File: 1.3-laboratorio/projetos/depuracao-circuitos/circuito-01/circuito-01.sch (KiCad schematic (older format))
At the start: 0 parts

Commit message: Atualização do projeto de depuração de circuitos
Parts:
- added D1: LED, LEDs:LED_D3.0mm, symbol LED
- added Entradas1: Conn_01x04, Connectors:Grove_1x04, symbol Conn_01x04
- added R1: R, Resistors_THT:R_Axial_DIN0309_L9.0mm_D3.2mm_P12.70mm_Horizontal, symbol R
- added U1: 74LS32, Housings_DIP:DIP-14_W7.62mm_Socket, symbol 74LS32
- added U2: 7400, Housings_DIP:DIP-14_W7.62mm_Socket, symbol 7400
- added U3: 74LS386, Housings_DIP:DIP-14_W7.62mm_Socket, symbol 74LS386
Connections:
- net labels added: GND
- wire segments 0 -> 47
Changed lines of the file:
@@
 Comment4 ""
 $EndDescr
+$Comp
+L GND #PWR01
+U 1 1 5B0DB24C
+P 9650 4150
+F 0 "#PWR01" H 9650 3900 50  0001 C CNN
+F 1 "GND" H 9650 4000 50  0000 C CNN
+F 2 "" H 9650 4150 50  0001 C CNN
+F 3 "" H 9650 4150 50  0001 C CNN
+	1    9650 4150
+	1    0    0    -1
+$EndComp
+$Comp
+L 7400 U2
+U 1 1 5B0DB2F1
+P 3650 3150
+F 0 "U2" H 3650 3200 50  0000 C CNN
+F 1 "7400" H 3650 3050 50  0000 C CNN
+F 2 "Housings_DIP:DIP-14_W7.62mm_Socket" H 3650 3150 50  0001 C CNN
+F 3 "" H 3650 3150 50  0001 C CNN
+	1    3650 3150
+	1    0    0    -1
+$EndComp
+$Comp
+L 7400 U2
+U 2 1 5B0DB37B
+P 5500 3900
+F 0 "U2" H 5500 3950 50  0000 C CNN
+F 1 "7400" H 5500 3800 50  0000 C CNN
+F 2 "Housings_DIP:DIP-14_W7.62mm_Socket" H 5500 3900 50  0001 C CNN
+F 3 "" H 5500 3900 50  0001 C CNN
+	2    5500 3900
+	1    0    0    -1
+$EndComp
+$Comp
+L 7400 U2
+U 3 1 5B0DB3EE
+P 6900 3900
+F 0 "U2" H 6900 3950 50  0000 C CNN
+F 1 "7400" H 6900 3800 50  0000 C CNN
+F 2 "Housings_DIP:DIP-14_W7.62mm_Socket" H 6900 3900 50  0001 C CNN
+F 3 "" H 6900 3900 50  0001 C CNN
+	3    6900 3900
+	1    0    0    -1
+$EndComp
+$Comp
+L 7400 U2
+U 4 1 5B0DB449
+P 7400 2900
+F 0 "U2" H 7400 2950 50  0000 C CNN
+F 1 "7400" H 7400 2800 50  0000 C CNN
+F 2 "Housings_DIP:DIP-14_W7.62mm_Socket" H 7400 2900 50  0001 C CNN
+F 3 "" H 7400 2900 50  0001 C CNN
+	4    7400 2900
+	1    0    0    -1
+$EndComp
+$Comp
+L 74LS32 U1
+U 1 1 5B0DB788
+P 3650 2450
+F 0 "U1" H 3650 2500 50  0000 C CNN
+F 1 "74LS32" H 3650 2400 50  0000 C CNN
+F 2 "Housings_DIP:DIP-14_W7.62mm_Socket" H 3650 2450 50  0001 C CNN
+F 3 "" H 3650 2450 50  0001 C CNN
+	1    3650 2450
+	1    0    0    -1
+$EndComp
+$Comp
+L 74LS32 U1
+U 2 1 5B0DB7F9
+P 3650 3900
+F 0 "U1" H 3650 3950 50  0000 C CNN
+F 1 "74LS32" H 3650 3850 50  0000 C CNN
+F 2 "Housings_DIP:DIP-14_W7.62mm_Socket" H 3650 3900 50  0001 C CNN
+F 3 "" H 3650 3900 50  0001 C CNN
+	2    3650 3900
+	1    0    0    -1
+$EndComp
+$Comp
+L 74LS32 U1
+U 3 1 5B0DB864
+P 5350 3150
+F 0 "U1" H 5350 3200 50  0000 C CNN
+F 1 "74LS32" H 5350 3100 50  0000 C CNN
+F 2 "Housings_DIP:DIP-14_W7.62mm_Socket" H 5350 3150 50  0001 C CNN
+F 3 "" H 5350 3150 50  0001 C CNN
+	3    5350 3150
+	1    0    0    -1
+$EndComp
+$Comp
+L 74LS386 U3
+U 1 1 5B0DB8C7
+P 8900 3300
+F 0 "U3" H 8900 3350 50  0000 C CNN
+F 1 "74LS386" H 8900 3250 50  0000 C CNN
+F 2 "Housings_DIP:DIP-14_W7.62mm_Socket" H 8900 3300 50  0001 C CNN
+F 3 "" H 8900 3300 50  0001 C CNN
+	1    8900 3300
+	1    0    0    -1
+$EndComp
+$Comp
+L Conn_01x04 Entradas1
+U 1 1 5B0DF1AF
+P 1600 2850
+F 0 "Entradas1" H 1600 3050 50  0000 C CNN
+F 1 "Conn_01x04" H 1600 2550 50  0000 C CNN
+F 2 "Connectors:Grove_1x04" H 1600 2850 50  0001 C CNN
+F 3 "" H 1600 2850 50  0001 C CNN
+	1    1600 2850
+	-1   0    0    -1
+$EndComp
+$Comp
+L LED D1
+U 1 1 5B0DF2B7
+P 9650 3900
+F 0 "D1" H 9650 4000 50  0000 C CNN
+F 1 "LED" H 9650 3800 50  0000 C CNN
+F 2 "LEDs:LED_D3.0mm" H 9650 3900 50  0001 C CNN
+F 3 "" H 9650 3900 50  0001 C CNN
+	1    9650 3900
+	0    -1   -1   0
+$EndComp
+$Comp
+L R R1
+U 1 1 5B0DF334
+P 9650 3500
+F 0 "R1" V 9730 3500 50  0000 C CNN
+F 1 "R" V 9650 3500 50  0000 C CNN
+F 2 "Resistors_THT:R_Axial_DIN0309_L9.0mm_D3.2mm_P12.70mm_Horizontal" V 9580 3500 50  0001 C CNN
+F 3 "" H 9650 3500 50  0001 C CNN
+	1    9650 3500
+	1    0    0    -1
+$EndComp
+Wire Wire Line
+	1800 2750 2350 2750
+Wire Wire Line
+	2350 2750 2350 2350
+Wire Wire Line
+	2350 2350 3050 2350
+Wire Wire Line
+	1800 2850 2500 2850
+Wire Wire Line
+	2500 2850 2500 2550
+Wire Wire Line
+	2500 2550 3050 2550
+Wire Wire Line
+	2900 2350 2900 3050
+Wire Wire Line
+	2900 3050 3050 3050
+Connection ~ 2900 2350
+Wire Wire Line
+	1800 2950 2750 2950
+Wire Wire Line
+	2750 2950 2750 3250
+Wire Wire Line
+	2750 3250 3050 3250
+Wire Wire Line
+	1800 3050 2600 3050
+Wire Wire Line
+	2600 3050 2600 4000
+Wire Wire Line
+	2600 4000 3050 4000
+Wire Wire Line
+	2700 2550 2700 3800
+Wire Wire Line
+	2700 3800 3050 3800
+Connection ~ 2700 2550
+Wire Wire Line
+	4250 3150 4500 3150
+Wire Wire Line
+	4500 3150 4500 3250
+Wire Wire Line
+	4500 3250 4750 3250
+Wire Wire Line
+	4750 3050 4750 2450
+Wire Wire Line
+	4250 2450 6150 2450
+Wire Wire Line
+	6800 2800 6150 2800
+Wire Wire Line
+	6150 2800 6150 2450
+Connection ~ 4750 2450
+Wire Wire Line
+	6800 3000 6300 3000
+Wire Wire Line
+	6300 3000 6300 3150
+Wire Wire Line
+	6300 3150 5950 3150
+Wire Wire Line
+	4250 3900 4450 3900
+Wire Wire Line
+	4450 3900 4450 4000
+Wire Wire Line
+	4450 4000 4900 4000
+Wire Wire Line
+	6250 3800 6250 4000
+Wire Wire Line
+	5300 3750 5350 3750
+Wire Wire Line
+	6250 4000 6300 4000
+Connection ~ 6250 3900
+Wire Wire Line
+	6150 3150 6150 3600
+Wire Wire Line
+	6150 3600 4900 3600
+Wire Wire Line
+	4900 3600 4900 3800
+Connection ~ 6150 3150
+Wire Wire Line
+	8300 3200 8200 3200
+Wire Wire Line
+	8200 3200 8200 2900
+Wire Wire Line
+	8200 2900 8000 2900
+Wire Wire Line
+	8300 3400 8200 3400
+Wire Wire Line
+	8200 3400 8200 3900
+Wire Wire Line
+	9650 3300 9650 3350
+Wire Wire Line
+	9650 3650 9650 3750
+Wire Wire Line
+	9650 4050 9650 4150
+Wire Wire Line
+	9650 3300 9500 3300
+Wire Wire Line
+	6300 3800 6250 3800
+Wire Wire Line
+	8200 3900 7500 3900
+Wire Wire Line
+	6250 3900 6100 3900
 $EndSCHEMATC

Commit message: Atualização no esquema/pcb
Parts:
- removed Entradas1: Conn_01x04, Connectors:Grove_1x04, symbol Conn_01x04
- added J?: Conn_02x04_Top_Bottom, symbol Conn_02x04_Top_Bottom
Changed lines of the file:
@@
-$EndComp
-$Comp
-L Conn_01x04 Entradas1
-U 1 1 5B0DF1AF
-P 1600 2850
-F 0 "Entradas1" H 1600 3050 50  0000 C CNN
-F 1 "Conn_01x04" H 1600 2550 50  0000 C CNN
-F 2 "Connectors:Grove_1x04" H 1600 2850 50  0001 C CNN
-F 3 "" H 1600 2850 50  0001 C CNN
-	1    1600 2850
-	-1   0    0    -1
 $EndComp
 $Comp
@@
 Wire Wire Line
 	6250 3900 6100 3900
+$Comp
+L Conn_02x04_Top_Bottom J?
+U 1 1 5B15FEC3
+P 1500 2850
+F 0 "J?" H 1550 3050 50  0000 C CNN
+F 1 "Conn_02x04_Top_Bottom" H 1550 2550 50  0000 C CNN
+F 2 "" H 1500 2850 50  0001 C CNN
+F 3 "" H 1500 2850 50  0001 C CNN
+	1    1500 2850
+	1    0    0    -1
+$EndComp
 $EndSCHEMATC

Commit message: Alteração PCB/Esquema elétrico
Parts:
- removed J?: Conn_02x04_Top_Bottom, symbol Conn_02x04_Top_Bottom
- added R2, R3, R4, R5: R, Resistors_THT:R_Axial_DIN0309_L9.0mm_D3.2mm_P12.70mm_Horizontal, symbol R
- added SW1: SW_DIP_x04, Buttons_Switches_THT:SW_DIP_x4_W7.62mm_Slide, symbol SW_DIP_x04
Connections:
- net labels added: +5V
- wire segments 47 -> 58
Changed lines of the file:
@@
 LIBS:contrib
 LIBS:valves
+LIBS:switches
 LIBS:circuito-01-cache
 EELAYER 25 0
@@
 $EndDescr
 $Comp
-L GND #PWR01
-U 1 1 5B0DB24C
-P 9650 4150
-F 0 "#PWR01" H 9650 3900 50  0001 C CNN
-F 1 "GND" H 9650 4000 50  0000 C CNN
-F 2 "" H 9650 4150 50  0001 C CNN
-F 3 "" H 9650 4150 50  0001 C CNN
-	1    9650 4150
-	1    0    0    -1
-$EndComp
-$Comp
 L 7400 U2
 U 1 1 5B0DB2F1
@@
 	1    0    0    -1
 $EndComp
+$Comp
+L GND #PWR01
+U 1 1 5B0DB24C
+P 9650 4150
+F 0 "#PWR01" H 9650 3900 50  0001 C CNN
+F 1 "GND" H 9650 4000 50  0000 C CNN
+F 2 "" H 9650 4150 50  0001 C CNN
+F 3 "" H 9650 4150 50  0001 C CNN
+	1    9650 4150
+	1    0    0    -1
+$EndComp
+$Comp
+L GND #PWR02
+U 1 1 5B1741D1
+P 1200 3250
+F 0 "#PWR02" H 1200 3000 50  0001 C CNN
+F 1 "GND" H 1200 3100 50  0000 C CNN
+F 2 "" H 1200 3250 50  0001 C CNN
+F 3 "" H 1200 3250 50  0001 C CNN
+	1    1200 3250
+	1    0    0    -1
+$EndComp
+$Comp
+L R R2
+U 1 1 5B174684
+P 1850 2000
+F 0 "R2" V 1930 2000 50  0000 C CNN
+F 1 "R" V 1850 2000 50  0000 C CNN
+F 2 "Resistors_THT:R_Axial_DIN0309_L9.0mm_D3.2mm_P12.70mm_Horizontal" V 1780 2000 50  0001 C CNN
+F 3 "" H 1850 2000 50  0001 C CNN
+	1    1850 2000
+	1    0    0    -1
+$EndComp
+$Comp
+L R R3
+U 1 1 5B174ABC
+P 2050 2000
+F 0 "R3" V 2130 2000 50  0000 C CNN
+F 1 "R" V 2050 2000 50  0000 C CNN
+F 2 "Resistors_THT:R_Axial_DIN0309_L9.0mm_D3.2mm_P12.70mm_Horizontal" V 1980 2000 50  0001 C CNN
+F 3 "" H 2050 2000 50  0001 C CNN
+	1    2050 2000
+	1    0    0    -1
+$EndComp
+$Comp
+L R R4
+U 1 1 5B174B13
+P 2250 2000
+F 0 "R4" V 2330 2000 50  0000 C CNN
+F 1 "R" V 2250 2000 50  0000 C CNN
+F 2 "Resistors_THT:R_Axial_DIN0309_L9.0mm_D3.2mm_P12.70mm_Horizontal" V 2180 2000 50  0001 C CNN
+F 3 "" H 2250 2000 50  0001 C CNN
+	1    2250 2000
+	1    0    0    -1
+$EndComp
+$Comp
+L R R5
+U 1 1 5B174B73
+P 2450 2000
+F 0 "R5" V 2530 2000 50  0000 C CNN
+F 1 "R" V 2450 2000 50  0000 C CNN
+F 2 "Resistors_THT:R_Axial_DIN0309_L9.0mm_D3.2mm_P12.70mm_Horizontal" V 2380 2000 50  0001 C CNN
+F 3 "" H 2450 2000 50  0001 C CNN
+	1    2450 2000
+	1    0    0    -1
+$EndComp
+$Comp
+L SW_DIP_x04 SW1
+U 1 1 5B174BFD
+P 1500 2950
+F 0 "SW1" H 1500 3300 50  0000 C CNN
+F 1 "SW_DIP_x04" H 1500 2700 50  0000 C CNN
+F 2 "Buttons_Switches_THT:SW_DIP_x4_W7.62mm_Slide" H 1500 2950 50  0001 C CNN
+F 3 "" H 1500 2950 50  0001 C CNN
+	1    1500 2950
+	1    0    0    -1
+$EndComp
+$Comp
+L +5V #PWR03
+U 1 1 5B175082
+P 2050 1650
+F 0 "#PWR03" H 2050 1500 50  0001 C CNN
+F 1 "+5V" H 2050 1790 50  0000 C CNN
+F 2 "" H 2050 1650 50  0001 C CNN
+F 3 "" H 2050 1650 50  0001 C CNN
+	1    2050 1650
+	1    0    0    -1
+$EndComp
 Wire Wire Line
 	1800 2750 2350 2750
@@
 Wire Wire Line
 	6250 3900 6100 3900
-$Comp
-L Conn_02x04_Top_Bottom J?
-U 1 1 5B15FEC3
-P 1500 2850
-F 0 "J?" H 1550 3050 50  0000 C CNN
-F 1 "Conn_02x04_Top_Bottom" H 1550 2550 50  0000 C CNN
-F 2 "" H 1500 2850 50  0001 C CNN
-F 3 "" H 1500 2850 50  0001 C CNN
-	1    1500 2850
-	1    0    0    -1
-$EndComp
+Wire Wire Line
+	1200 2750 1200 3250
+Connection ~ 1200 2950
+Wire Wire Line
+	1200 2850 1200 2950
+Connection ~ 1200 2850
+Connection ~ 1200 3050
+Wire Wire Line
+	1850 1650 2450 1650
+Wire Wire Line
+	2450 1650 2450 1850
+Wire Wire Line
+	2250 1650 2250 1850
+Wire Wire Line
+	2050 1850 2050 1650
+Wire Wire Line
+	1850 1850 1850 1650
+Connection ~ 2050 1650
+Wire Wire Line
+	1850 2150 1850 2750
+Connection ~ 1850 2750
+Wire Wire Line
+	2050 2150 2050 2850
+Connection ~ 2050 2850
+Wire Wire Line
+	2250 2150 2250 2950
+Connection ~ 2250 2950
+Wire Wire Line
+	2450 2150 2450 3050
+Connection ~ 2450 3050
 $EndSCHEMATC

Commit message: Revisões no esquemático e proposta de novo leiaute da placa.
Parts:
- added P1: CONN_01X02, Terminal_Blocks:TerminalBlock_Altech_AK300-2_P5.00mm, symbol CONN_01X02
- R1, R2, R3, R4, R5: footprint Resistors_THT:R_Axial_DIN0309_L9.0mm_D3.2mm_P12.70mm_Horizontal -> Resistors_ThroughHole:R_Axial_DIN0207_L6.3mm_D2.5mm_P10.16mm_Horizontal
- SW1: footprint Buttons_Switches_THT:SW_DIP_x4_W7.62mm_Slide -> Buttons_Switches_ThroughHole:SW_DIP_x4_W7.62mm_Slide
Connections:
- net labels added: VCC
- net labels removed: +5V
- wire segments 58 -> 61
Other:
- note added: "(+5V)"
- moved on the sheet: D1, R1, R2, R3, R4, R5, SW1, U1A, U1B, U1C, U2A, U2B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

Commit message: Símbolo do LED alterado.
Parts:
- removed D1: LED, LEDs:LED_D3.0mm, symbol LED
- added D1: LED_ALT, symbol LED_ALT
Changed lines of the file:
@@
 EESchema Schematic File Version 2
+LIBS:circuito-01-rescue
 LIBS:power
 LIBS:device
@@
 $EndComp
 $Comp
-L LED D1
-U 1 1 5B0DF2B7
-P 9800 4400
-F 0 "D1" H 9800 4500 50  0000 C CNN
-F 1 "LED" H 9800 4300 50  0000 C CNN
-F 2 "LEDs:LED_D3.0mm" H 9800 4400 50  0001 C CNN
-F 3 "" H 9800 4400 50  0001 C CNN
-	1    9800 4400
-	0    -1   -1   0
-$EndComp
-$Comp
 L R R1
 U 1 1 5B0DF334
@@
 	5800 4450 5850 4450
 Wire Wire Line
-	9800 4150 9800 4200
-Wire Wire Line
-	9800 4600 9800 4650
+	9800 4150 9800 4250
+Wire Wire Line
+	9800 4550 9800 4650
 Wire Wire Line
 	5800 4250 5850 4250
@@
 	2200 2900 2200 2850
 Connection ~ 2200 2850
+$Comp
+L LED_ALT D1
+U 1 1 5B295E8B
+P 9800 4400
+F 0 "D1" H 9800 4500 50  0000 C CNN
+F 1 "LED_ALT" H 9800 4300 50  0001 C CNN
+F 2 "" H 9800 4400 50  0001 C CNN
+F 3 "" H 9800 4400 50  0001 C CNN
+	1    9800 4400
+	0    -1   -1   0
+$EndComp
 $EndSCHEMATC

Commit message: Em complementação o Circuito 01 para depuração.
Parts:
- added J1, J2, J3, J4, J5, J6: Conn_01x07_Male, symbol Connector:Conn_01x07_Male
- D1: symbol LED_ALT -> circuito-01-rescue:LED_ALT
- P1: symbol CONN_01X02 -> circuito-01-rescue:CONN_01X02
- R1, R2, R3, R4, R5: symbol R -> circuito-01-rescue:R
- SW1: symbol SW_DIP_x04 -> circuito-01-rescue:SW_DIP_x04
- U1: footprint Housings_DIP:DIP-14_W7.62mm_Socket -> Package_DIP:DIP-14_W7.62mm_LongPads; symbol 74LS32 -> circuito-01-rescue:74LS32
- U2: footprint Housings_DIP:DIP-14_W7.62mm_Socket -> Package_DIP:DIP-14_W7.62mm_LongPads; symbol 7400 -> circuito-01-rescue:7400
- U3: footprint Housings_DIP:DIP-14_W7.62mm_Socket -> Package_DIP:DIP-14_W7.62mm_LongPads; symbol 74LS386 -> circuito-01-rescue:74LS386
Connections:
- net labels added: U1-01, U1-02, U1-03, U1-04, U1-05, U1-06, U1-07, U1-08, U1-09, U1-10, U1-11, U1-12, U1-13, U1-14, U2-01, U2-02, U2-03, U2-04, U2-05, U2-06, U2-07, U2-08, U2-09, U2-10, U2-11, U2-12, U2-13, U2-14, U3-01, U3-02, U3-03, U3-04, U3-05, U3-06, U3-07, U3-08, U3-09, U3-10, U3-11, U3-12, U3-13, U3-14
- wire segments 61 -> 120
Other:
- moved on the sheet: D1, P1, R1, R2, R3, R4, R5, SW1, U1A, U1B, U1C, U2A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

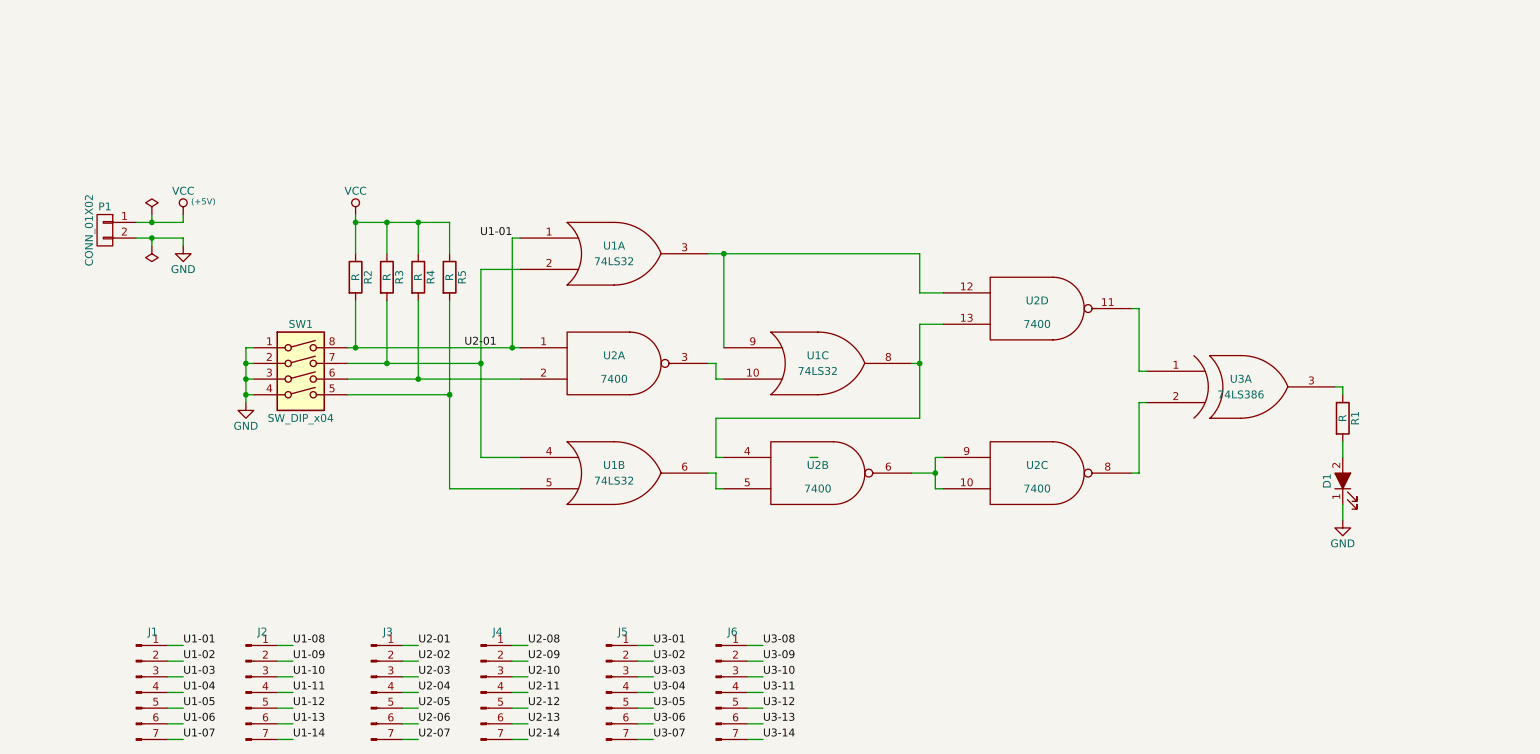
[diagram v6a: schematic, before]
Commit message: Concluída a revisão do esquemático para o circuito de depuração Circuito 01.
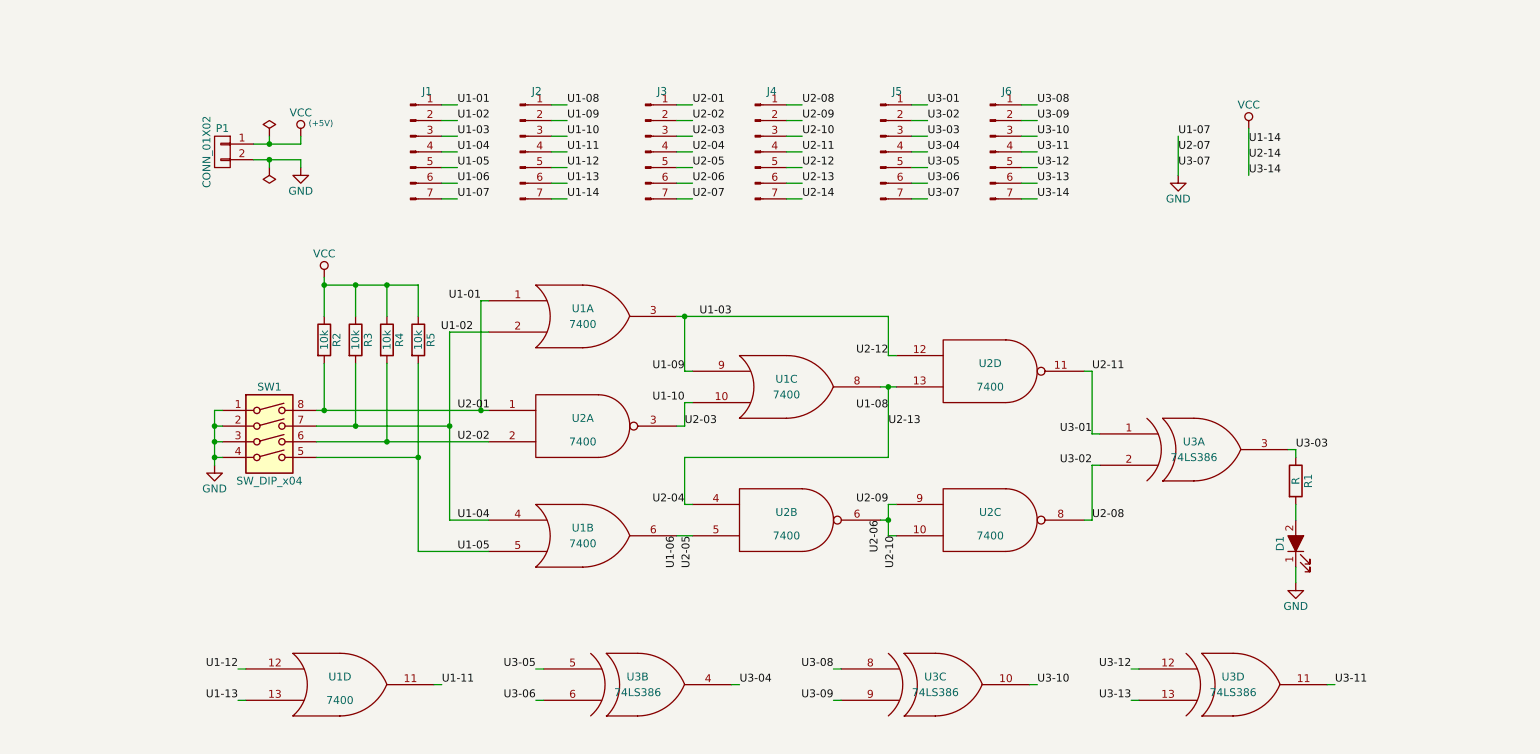
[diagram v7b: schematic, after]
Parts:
- added unit 4 of U1
- added unit 2 of U3
- added unit 3 of U3
- added unit 4 of U3
- R2, R3, R4, R5: value R -> 10k
- U1: value 74LS32 -> 7400
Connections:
- net U1-04 is gone; now on net U1-02: J1.4 (Pin_4)
- net U1-07 is gone; now on net GND: J1.7 (Pin_7)
- net U1-09 is gone; now on net U1-03: J2.2 (Pin_2)
- net U1-14 is gone; now on net VCC: J2.7 (Pin_7)
- net U2-03 is gone; now on net U1-10: J3.3 (Pin_3)
- net U2-04 is gone; now on net U1-08: J3.4 (Pin_4)
- net U2-05 is gone; now on net U1-06: J3.5 (Pin_5)
- net U2-07 is gone; now on net GND: J3.7 (Pin_7)
- net U2-09 is gone; now on net U2-06: J4.2 (Pin_2)
- net U2-10 is gone; now on net U2-06: J4.3 (Pin_3)
- net U2-12 is gone; now on net U1-03: J4.5 (Pin_5)
- net U2-13 is gone; now on net U1-08: J4.6 (Pin_6)
- net U2-14 is gone; now on net VCC: J4.7 (Pin_7)
- net U3-01 is gone; now on net U2-11: J5.1 (Pin_1)
- net U3-02 is gone; now on net U2-08: J5.2 (Pin_2)
- net U3-07 is gone; now on net GND: J5.7 (Pin_7)
- net U3-14 is gone; now on net VCC: J6.7 (Pin_7)
- net GND: now also U1.7 (GND), U3.7 (GND), U3.7 (GND), U3.7 (GND)
- net U1-02: now also R3.2, SW1.7, U1.2, U1.4
- net U1-03: now also U1.3, U1.9, U2.12
- net U1-05: now also R5.2, SW1.5, U1.5
- net U1-06: now also U1.6, U2.5
- net U1-08: now also U1.8, U2.13, U2.4
- net U1-10: now also U1.10, U2.3
- net U1-11: now also U1.11
- net U1-12: now also U1.12
- net U1-13: now also U1.13
- net U2-02: now also R4.2, SW1.6, U2.2
- net U2-06: now also U2.10, U2.6, U2.9
- net U2-08: now also U2.8, U3.2
- net U2-11: now also U2.11, U3.1
- net U3-03: now also R1.1, U3.3
- net U3-04: now also U3.4
- net U3-05: now also U3.5
- net U3-06: now also U3.6
- net U3-08: now also U3.8
- net U3-09: now also U3.9
- net U3-10: now also U3.10
- net U3-11: now also U3.11
- net U3-12: now also U3.12
- net U3-13: now also U3.13
- net VCC: now also U1.14 (VCC), U3.14 (VCC), U3.14 (VCC), U3.14 (VCC)
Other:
- moved on the sheet: D1, J1, J2, J3, J4, J5, J6, P1, R1, R2, R3, R4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
